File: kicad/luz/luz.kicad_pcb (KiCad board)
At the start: 4 copper layers, 49.4 x 21.9 mm, 67 parts, among them J2 Screw_Terminal_01x04, Q1 AO3400A, Q4 AO3400A, U1 U261-241N-4BS2SS, U2 CYPD3177-24LQXQ_C2959321, U3 SI4909DY-VB, U4 TPS54302, U5 ESP32-WROOM-32D

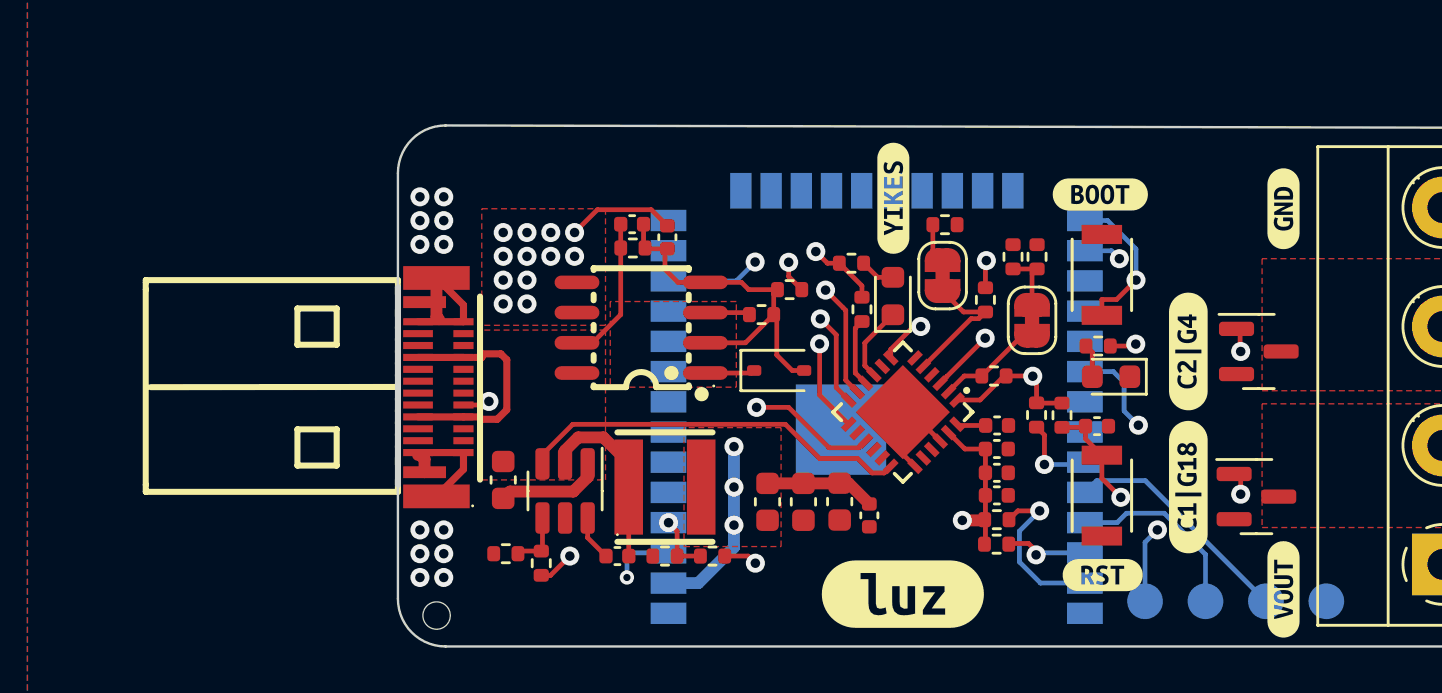
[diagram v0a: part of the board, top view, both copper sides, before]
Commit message: Adds 470 resistors to N FET channel drivers' gates & fix VBUSMAX
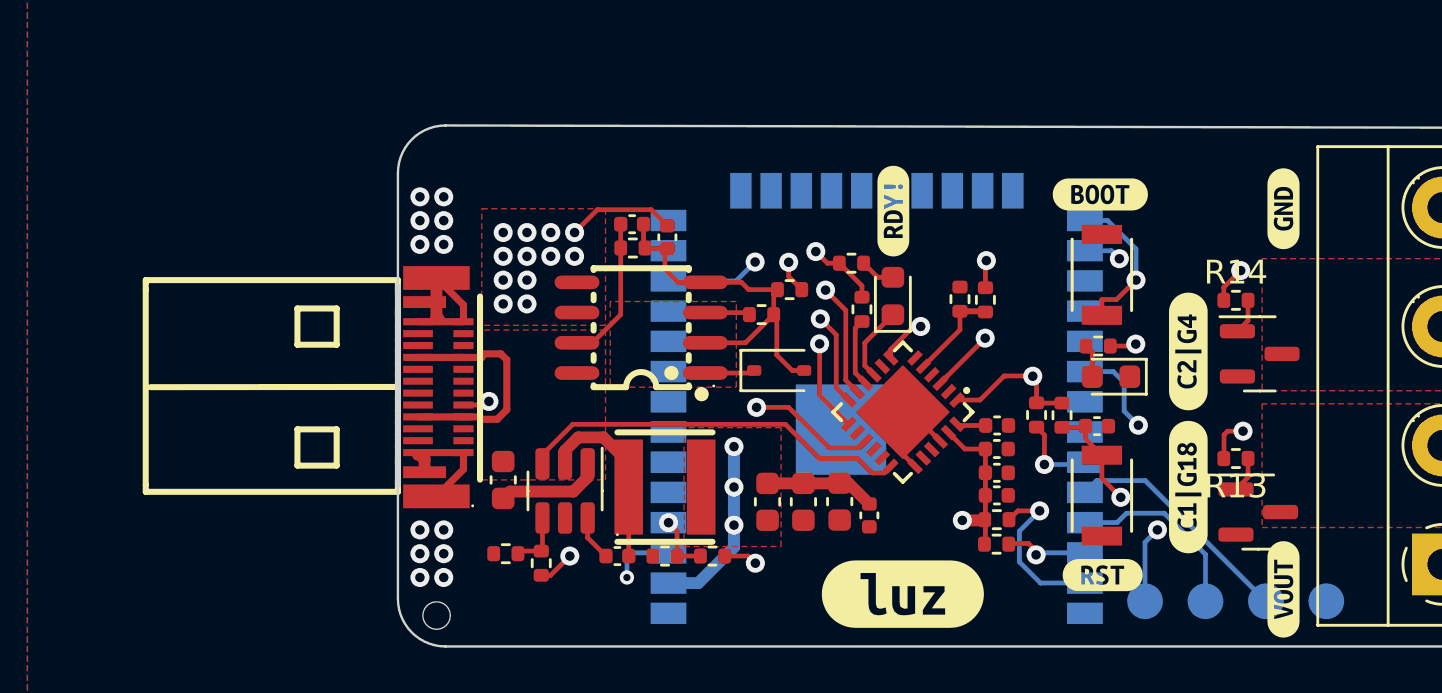
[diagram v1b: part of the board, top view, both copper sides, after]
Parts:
- removed JP1: 12V, Jumper:SolderJumper-2_P1.3mm_Bridged_RoundedPad1.0x1.5mm
- removed JP2: 3A/5A, Jumper:SolderJumper-2_P1.3mm_Bridged_RoundedPad1.0x1.5mm
- removed R17, R18, R19: 10k, Resistor_SMD:R_0402_1005Metric
- removed kibuzzard-655BC300: G***, kibuzzard-655BC300
- added R13: 470, Resistor_SMD:R_0402_1005Metric, F.Cu at (67.8, 110.0)
- added R14: 470, Resistor_SMD:R_0402_1005Metric, F.Cu at (67.8, 103.3)
- added kibuzzard-658ADB24: G***, kibuzzard-658ADB24, F.Cu at (53.4, 99.6)
- moved R22 3.19 mm to (56.2, 103.3), turned to 90 degrees
- moved Q4 0.65 mm to (68.7, 112.2)
- moved Q1 0.11 mm to (68.8, 105.6)
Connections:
- R22 pad 1: Net-(JP2-A) -> ICOA
- U2 pad 2: VBMAX -> GND
- U5 pad 26: C2 -> Net-(U5-IO4)
- U5 pad 30: C1 -> Net-(U5-IO18)
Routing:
- net Net-(U5-IO18): track 0.00 -> 10.3 mm, vias 0 -> 2
- net C1: track 10.3 -> 1.51 mm, vias 2 -> 0
- net Net-(U5-IO4): track 0.00 -> 8.44 mm, vias 0 -> 2
- net C2: track 9.26 -> 1.49 mm, vias 2 -> 0
- net VBMAX: track 4.48 -> 0.00 mm
- net Net-(JP1-A): track 2.61 -> 0.00 mm
- net ICOA: track 5.72 -> 4.04 mm
- net Net-(JP2-A): track 1.66 -> 0.00 mm

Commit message: Plotted fab outputs for 0.0.3a
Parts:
- removed kibuzzard-655BB508: G***, kibuzzard-655BB508
- added kibuzzard-658AE32D: G***, kibuzzard-658AE32D, B.Cu at (72.2, 103.6)
- added kibuzzard-658AE3F9: G***, kibuzzard-658AE3F9, B.Cu at (70.2, 103.6)
